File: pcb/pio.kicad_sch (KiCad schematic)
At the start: 27 parts, among them J4 GPB[0..3], J5 GPB[4..7], J6 BTN_IN, J7 GPA[4..7], U4 MCP23017_ML

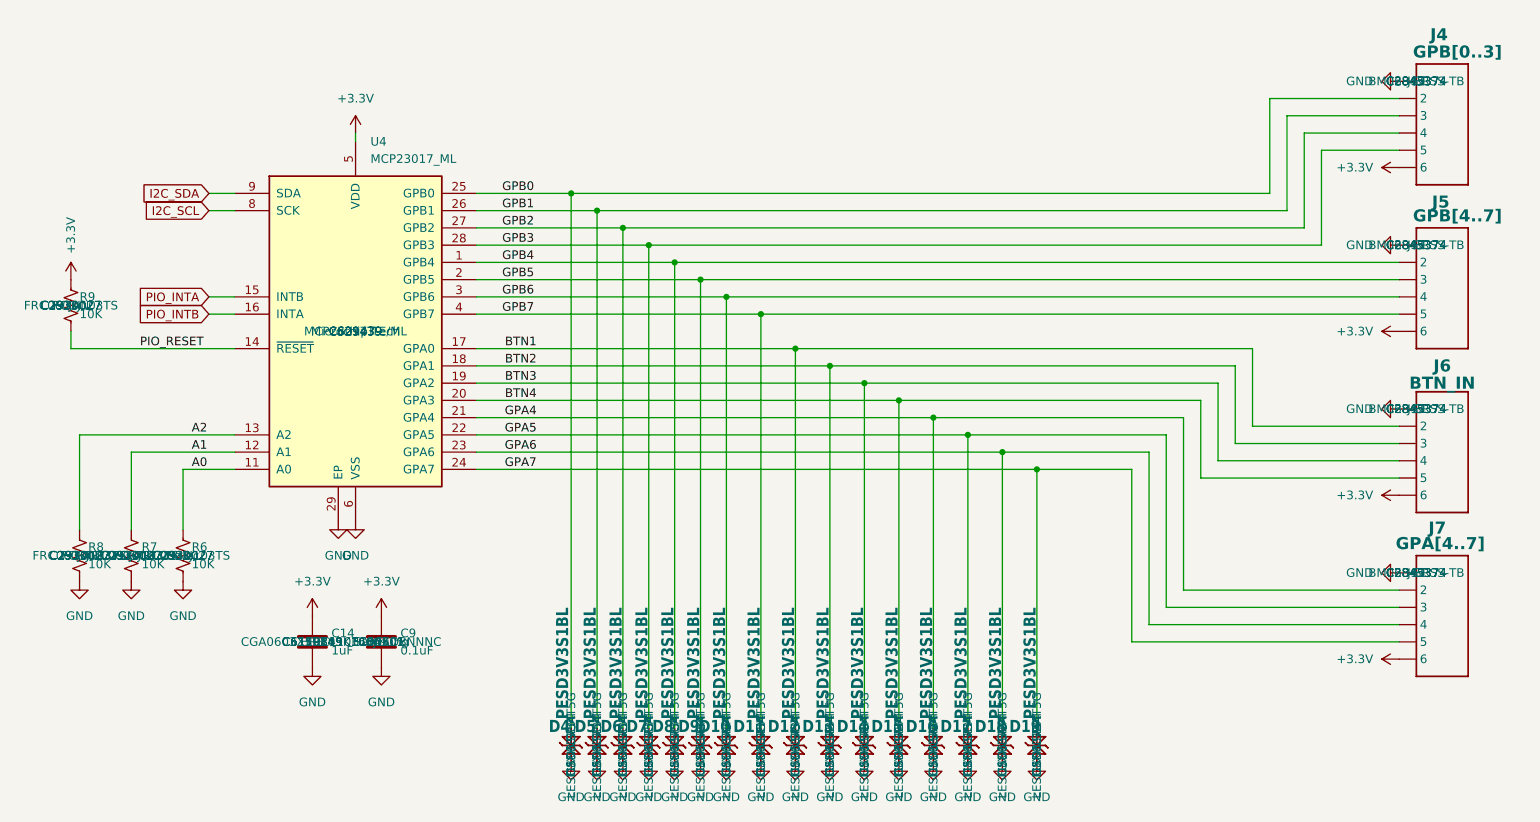
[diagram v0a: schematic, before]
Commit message: Changed SPI to 8 pin connector
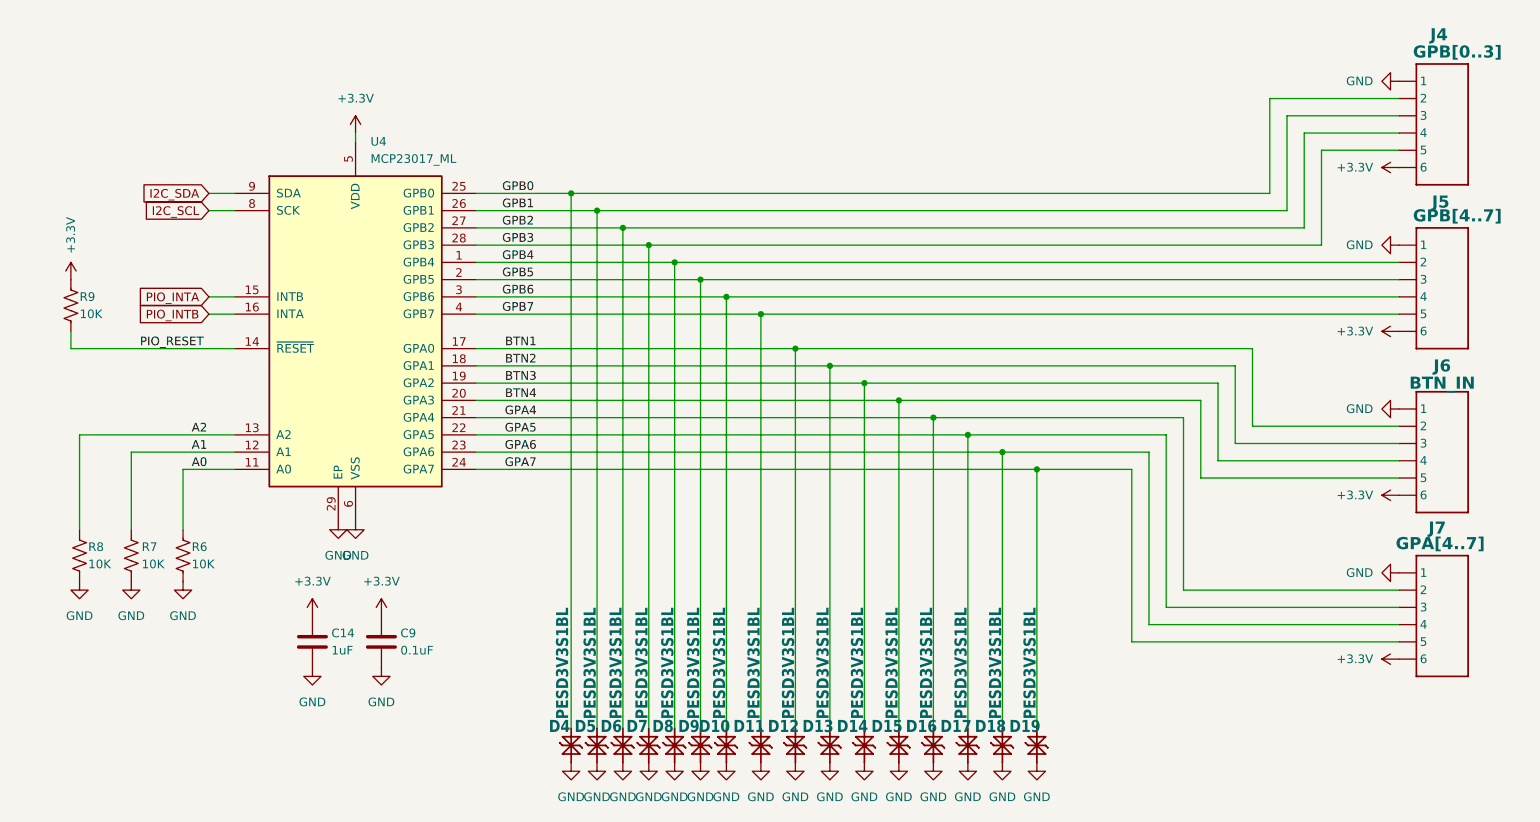
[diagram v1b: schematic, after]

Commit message: Added additional labels; minor clean up.
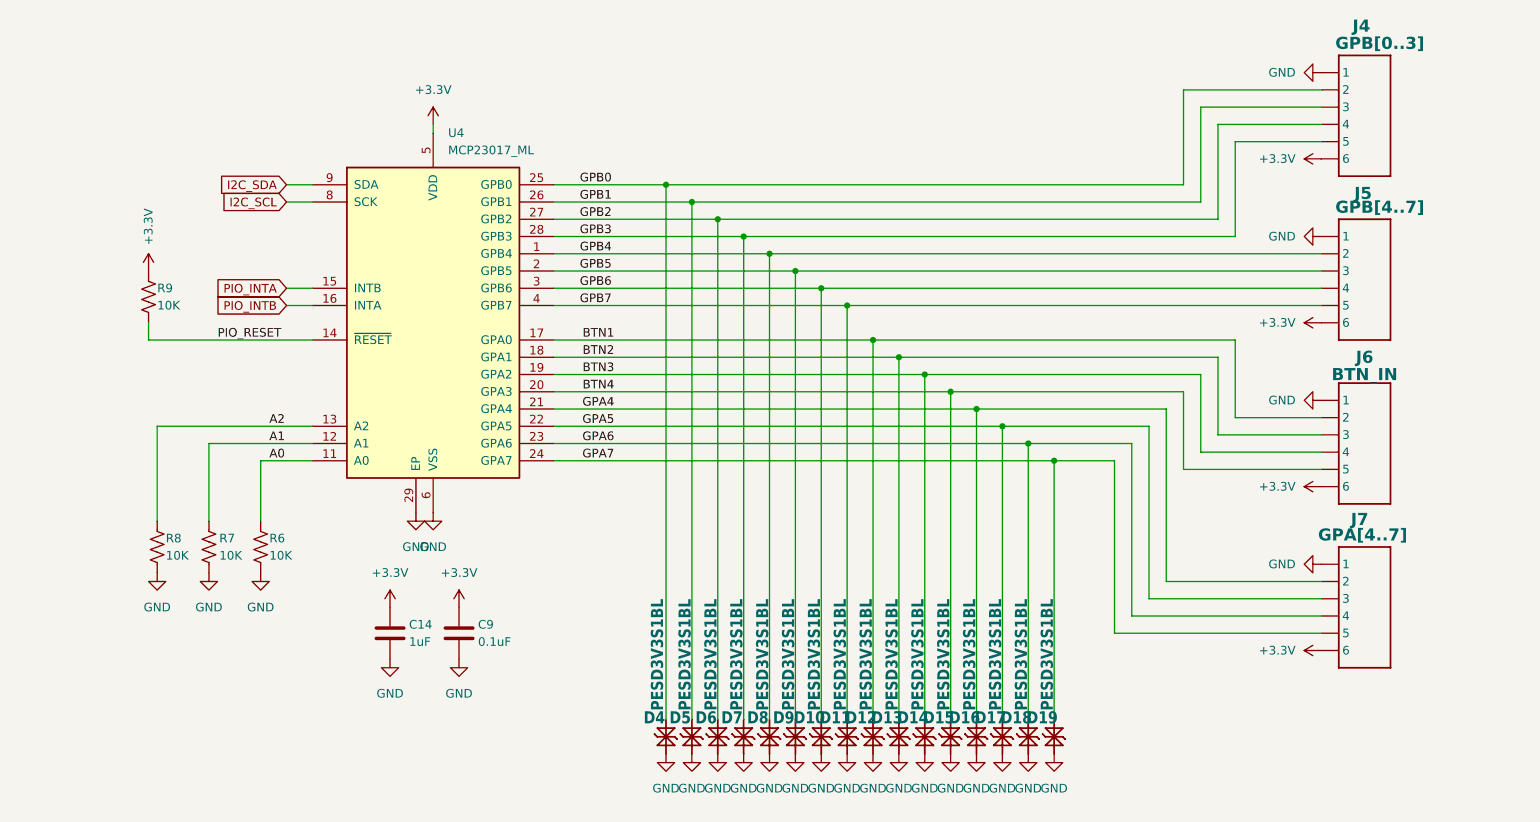
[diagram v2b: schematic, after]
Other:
- moved on the sheet: C14, C9, D10, D11, D12, D13, D14, D15, D16, D17, D18, D19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

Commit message: added open hw; changed test points; added pulls on buttons
change buttons to be 2 connectors with pull ups.
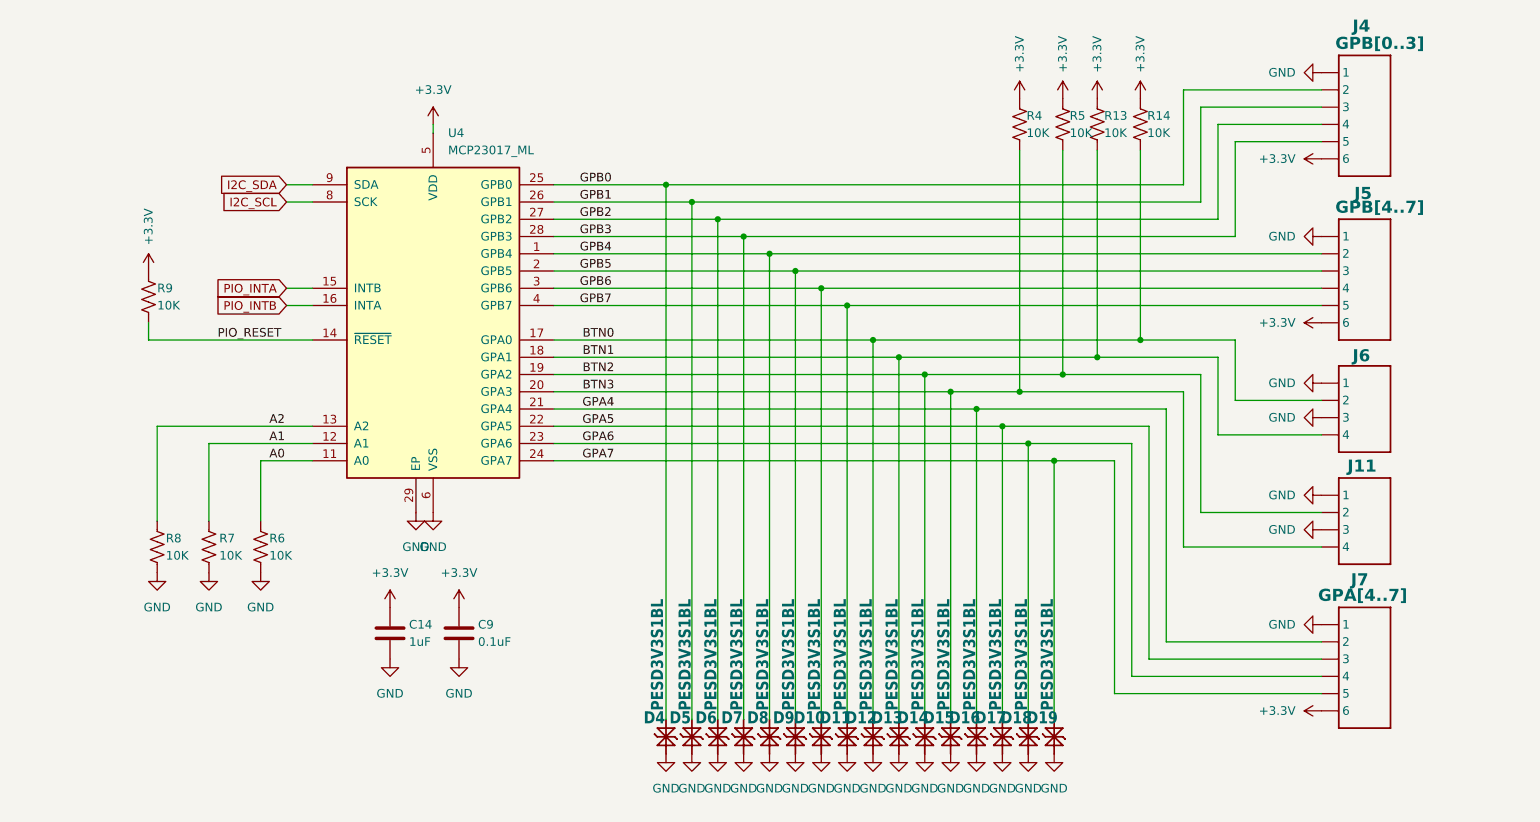
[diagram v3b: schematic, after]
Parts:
- removed J6: BTN_IN, CRGM Connector:JST_SH_BM06B-SRSS-TB_1x06-1MP_P1.00mm_Vertical, symbol CRGM Connector:JST-SH-6
- added J11, J6: ~, CRGM Connector:JST_SH_BM04B-SRSS-TB_1x04-1MP_P1.00mm_Vertical, symbol CRGM Connector:JST-SH-4
- added R13, R14, R4, R5: 10K, Resistor_SMD:R_0603_1608Metric, symbol Device:R_US
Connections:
- net BTN4 is gone; now on net BTN3: D15.2 (K2), U4.20 (GPA3)
- net +3.3V: now also R13.1, R14.1, R4.1, R5.1
- net BTN1: now also D13.2 (K2), U4.18 (GPA1), J6.4, R13.2; no longer D12.2 (K2), U4.17 (GPA0)
- net BTN2: now also D14.2 (K2), U4.19 (GPA2), J11.2, R5.2; no longer D13.2 (K2), U4.18 (GPA1)
- net BTN3: now also J11.4, R4.2; no longer D14.2 (K2), U4.19 (GPA2)
- net GND: now also J11.1, J11.3, J6.1, J6.3
- new net BTN0: D12.2 (K2), J6.2, R14.2, U4.17 (GPA0)
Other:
- moved on the sheet: J7

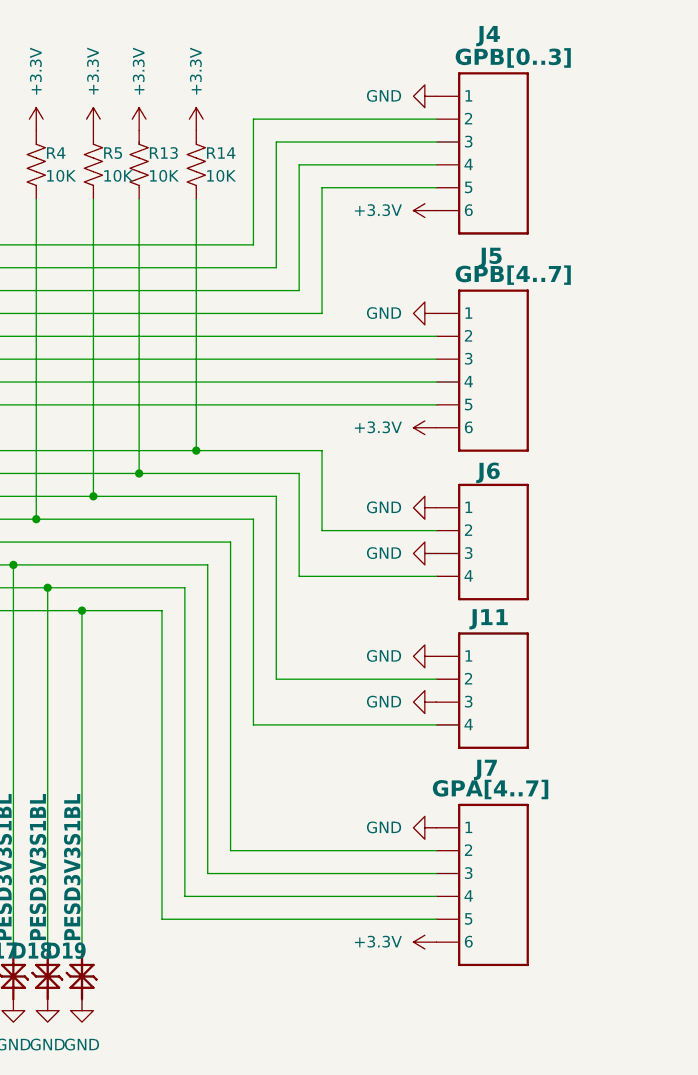
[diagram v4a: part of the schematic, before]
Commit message: Major overhaul of IO
Added GPIO module
Added SPI interface
Added serial interface
Added power selection
Added power LEDs
Changed v3.3 LDO
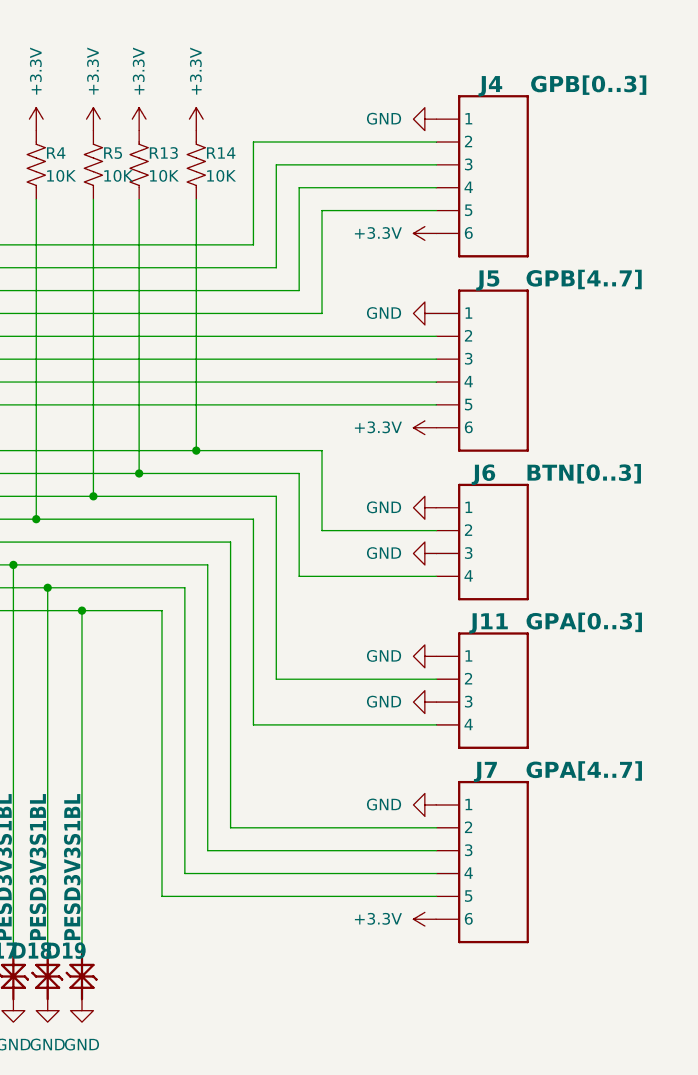
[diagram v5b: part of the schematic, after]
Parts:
- J11: value ~ -> GPA[0..3]
- J6: value ~ -> BTN[0..3]
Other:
- moved on the sheet: J4, J7

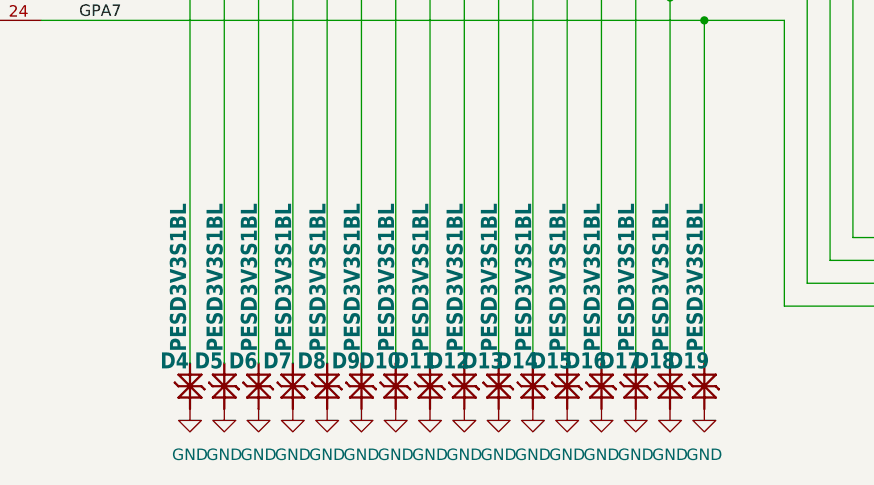
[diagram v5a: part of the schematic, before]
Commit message: Fixed MPN mismatches and other fields
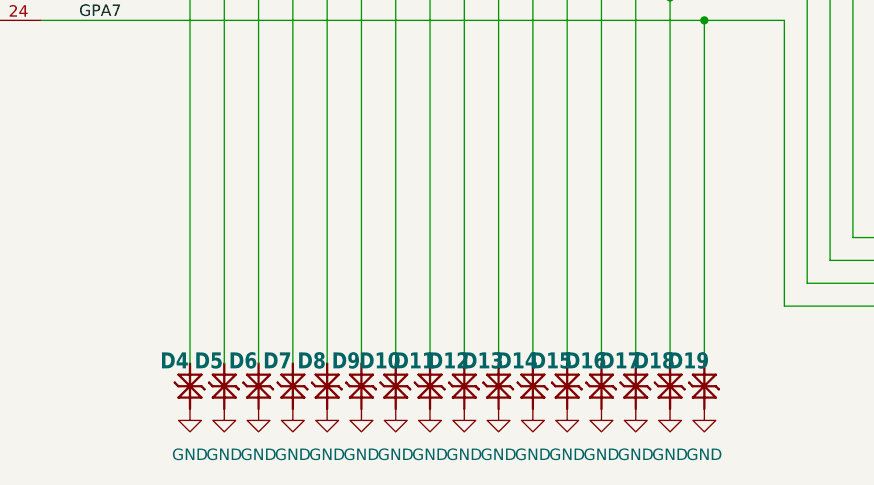
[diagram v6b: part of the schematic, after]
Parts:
- J11, J6: MF (none) -> JST
- J4, J5, J7: MPN BM06B-SRSS-TB -> BM06B-SRSS-TB
- R6: MN Ralec -> FOJAN

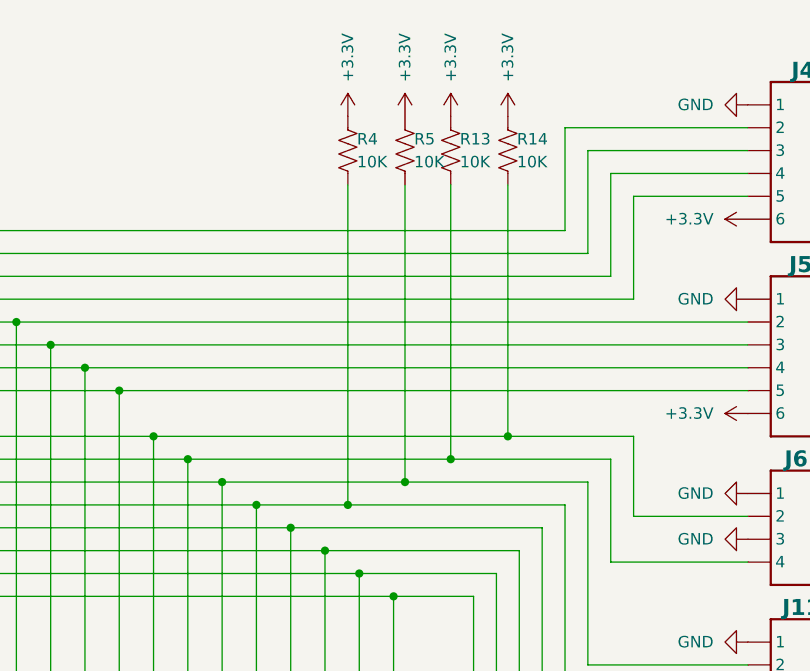
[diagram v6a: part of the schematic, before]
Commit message: Removed duplicative ESB on USB
Updated descriptions for consistency
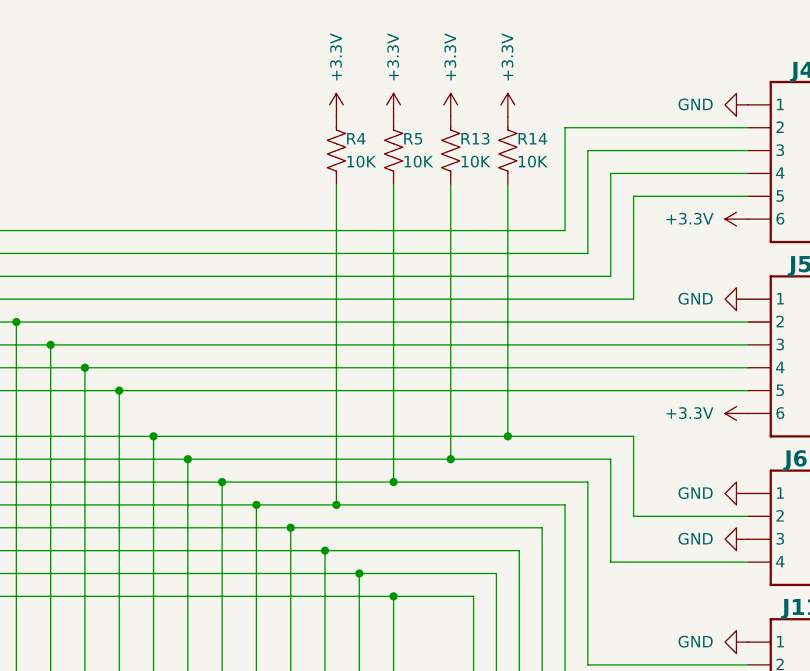
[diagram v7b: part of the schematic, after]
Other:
- moved on the sheet: R4, R5

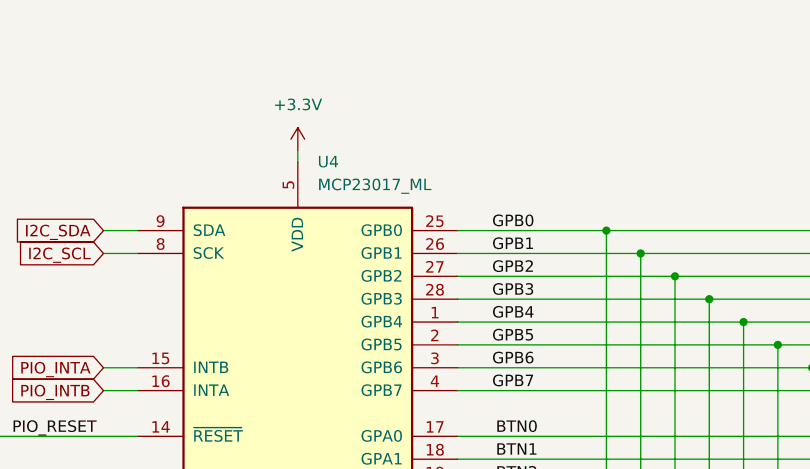
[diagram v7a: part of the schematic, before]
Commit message: Fixed cap values on reset button
Fixed all part numbers and extended parameters.
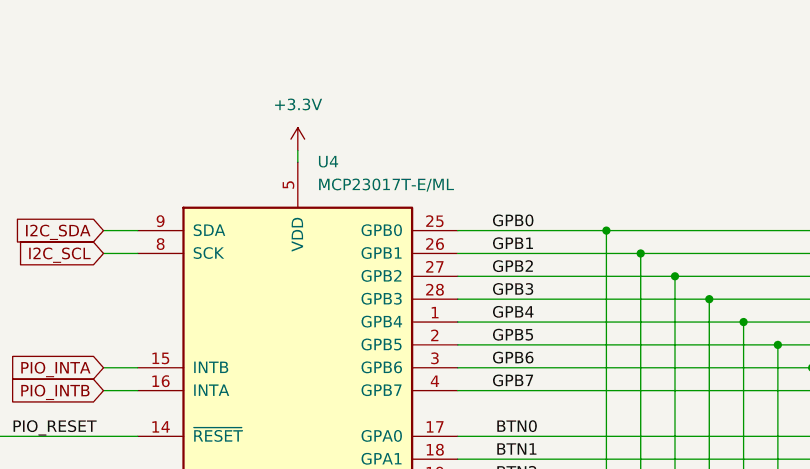
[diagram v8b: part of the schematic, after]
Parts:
- C14: Digikey (none) -> 1276-1019-2-ND; LCSC_PN C6119849 -> (none); MF HRE -> (none); Mouser (none) -> 187-CL10B105KO8NNNC
- C9: Digikey (none) -> 1276-1005-2-ND; LCSC_PN C66501 -> (none); MF Samsung -> (none); Mouser (none) -> 187-CL10B104KO8NNNC
- D10, D11, D12, D13, D14, D15, D16, D17, D18, D19, D4, D5, D6, D7, D8, D9: Digikey (none) -> 1727-PESD3V3S1BLYLTR-ND; LCSC_PN C5563754 -> (none); MF FUXINSEMI -> (none); Mouser (none) -> 621-DESD3V3S1BL-7B
- J11, J6: MF JST -> (none)
- J4, J5, J7: Digikey (none) -> 455-BM06B-SRSS-TBTR-ND; LCSC_PN C2845374 -> (none); MF JST -> (none); Mouser (none) -> 306-BM06BSRSSTBTLFSN
- R13, R14, R4, R5, R6, R7, R8, R9: Digikey (none) -> CR0603-JW-103ELFTR-ND; LCSC_PN C2930027 -> (none); MF FOJAN -> (none); Mouser (none) -> 652-CR0603-JW-103ELF
- U4: value MCP23017_ML -> MCP23017T-E/ML; Digikey (none) -> MCP23017-E/ML-ND; LCSC_PN C629439 -> (none); MF Microchip Tech -> (none); Mouser (none) -> 579-MCP23017-E/ML
